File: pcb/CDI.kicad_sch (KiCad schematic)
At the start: 32 parts, among them Q1 MMBT2222A, Q10 MMBTA55, Q5 MMBT2222A, Q6 MMBT2222A, Q8 MMBTA55, Q9 MMBTA55

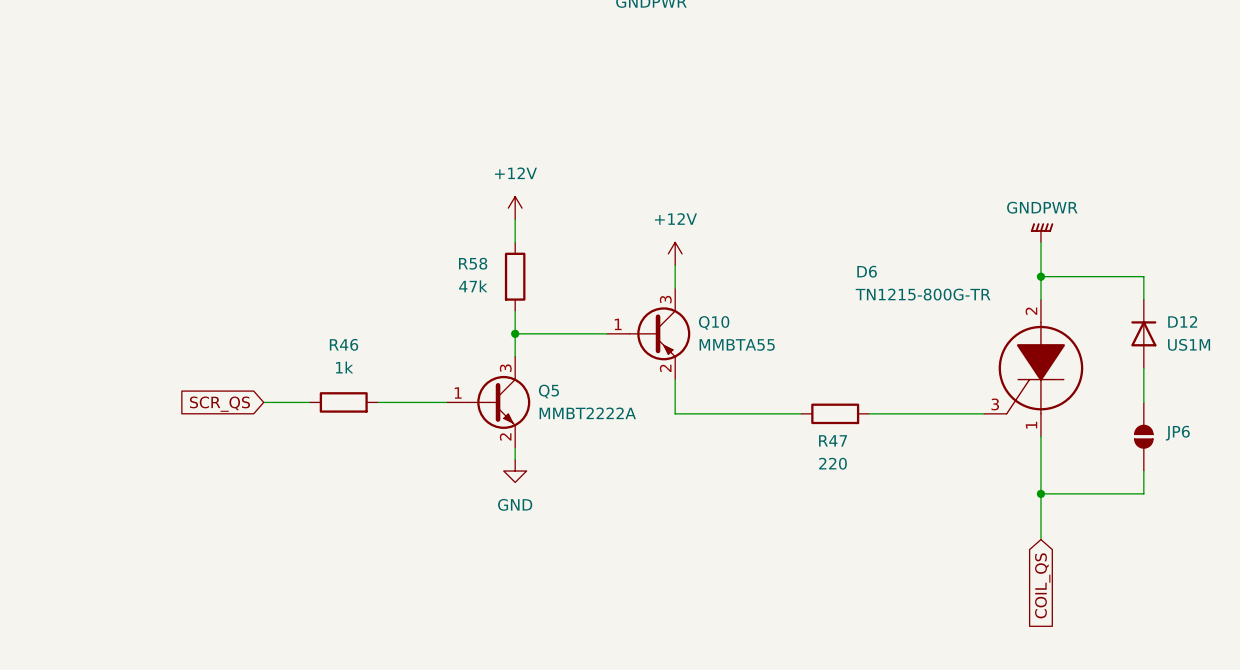
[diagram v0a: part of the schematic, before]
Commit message: changed the QS cut to use a relay
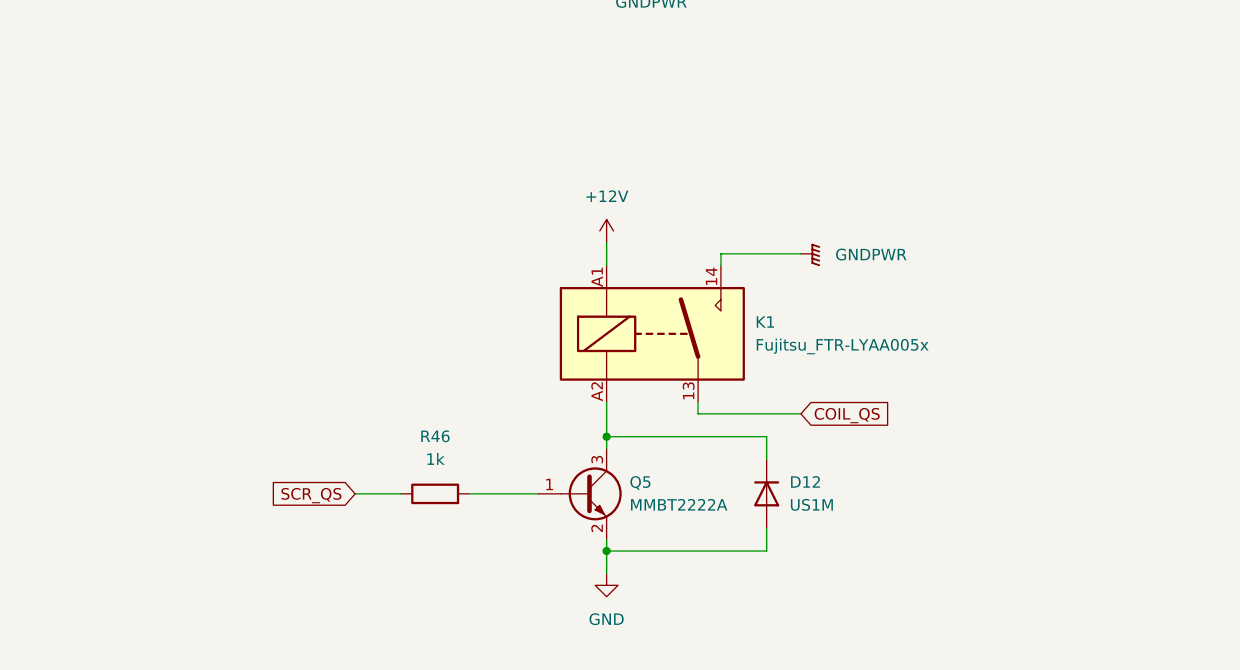
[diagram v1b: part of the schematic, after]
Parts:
- removed D6: TN1215-800G-TR, SamacSys_Parts:TN1215800GTR, symbol SamacSys_Parts:TN1215-800G-TR
- removed JP6: SolderJumper_2_Open, Jumper:SolderJumper-2_P1.3mm_Open_RoundedPad1.0x1.5mm, symbol Jumper:SolderJumper_2_Open
- removed Q10: MMBTA55, Package_TO_SOT_SMD:SOT-23, symbol Transistor_BJT:MMBTA56
- removed R47: 220, Resistor_THT:R_Axial_DIN0204_L3.6mm_D1.6mm_P1.90mm_Vertical, symbol Device:R
- removed R58: 47k, Resistor_THT:R_Axial_DIN0204_L3.6mm_D1.6mm_P1.90mm_Vertical, symbol Device:R
- added K1: Fujitsu_FTR-LYAA005x, Relay_THT:Relay_SPST-NO_Fujitsu_FTR-LYAA005x_FormA_Vertical, symbol Relay:Fujitsu_FTR-LYAA005x
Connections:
- net +12V: now also K1.A1
- net COIL_QS: now also K1.13
- net GND: now also D12.2 (A)
- net GNDPWR: now also K1.14; no longer D12.1 (K)
- net at Q5.3 (C): now also D12.1 (K), K1.A2
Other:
- moved on the sheet: D12, Q5, R46

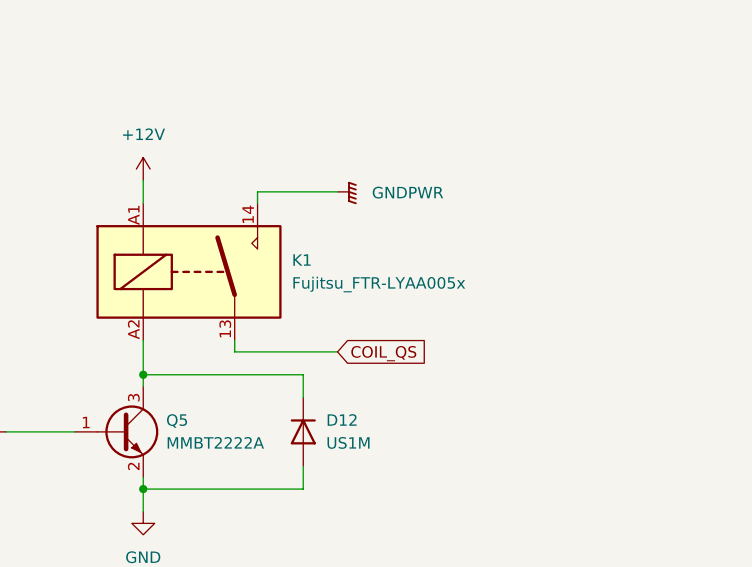
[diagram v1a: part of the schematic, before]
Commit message: added custom footprint for external relay
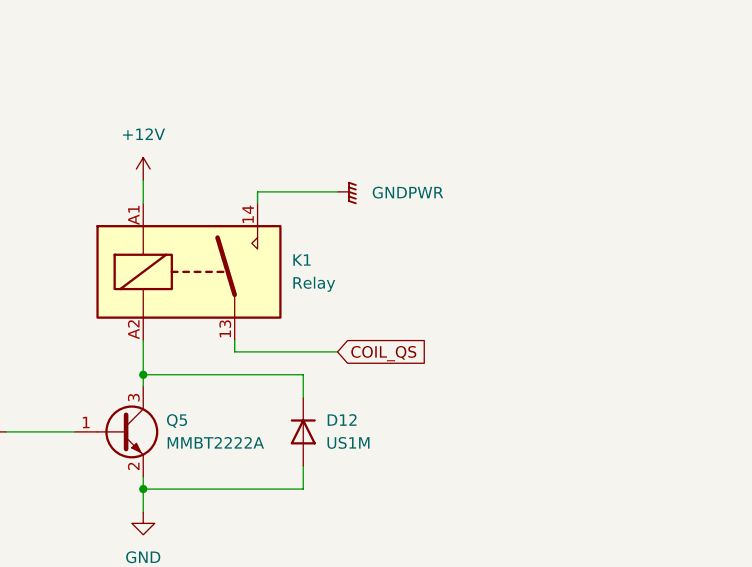
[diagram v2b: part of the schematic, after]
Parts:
- K1: value Fujitsu_FTR-LYAA005x -> Relay; footprint Relay_THT:Relay_SPST-NO_Fujitsu_FTR-LYAA005x_FormA_Vertical -> Custom:Ext_Relay
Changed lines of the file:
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@@
 			)
 		)
-		(property "Value" "Fujitsu_FTR-LYAA005x"
+		(property "Value" "Relay"
 			(at 220.98 125.7299 0)
 			(effects
@@
 			)
 		)
-		(property "Footprint" "Relay_THT:Relay_SPST-NO_Fujitsu_FTR-LYAA005x_FormA_Vertical"
+		(property "Footprint" "Custom:Ext_Relay"
 			(at 220.98 125.73 0)
 			(effects

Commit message: added DNP for fabrication and 2P molex connector, minor fixes
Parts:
- removed R57: 10k, Resistor_THT:R_Axial_DIN0204_L3.6mm_D1.6mm_P1.90mm_Vertical, symbol Device:R
- added R45: 10k, Resistor_SMD:R_0603_1608Metric, symbol Device:R
- added TP30, TP31: TestPoint, Connector_PinHeader_2.54mm:PinHeader_1x01_P2.54mm_Vertical, symbol Connector:TestPoint
- R13, R49, R56: footprint Resistor_THT:R_Axial_DIN0204_L3.6mm_D1.6mm_P1.90mm_Vertical -> Resistor_SMD:R_0603_1608Metric
- TP10, TP11, TP19, TP9: footprint Connector_PinHeader_1.00mm:PinHeader_1x01_P1.00mm_Vertical -> Connector_PinHeader_2.54mm:PinHeader_1x01_P2.54mm_Vertical; now not fitted
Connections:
- net +12V: now also R45.1
- net COIL_QS: now also TP31.1
- net KILL_SWITCH: now also TP30.1
- net at D13.3: now also R56.2; no longer R56.1
- net at Q1.3 (C), Q9.1 (B): now also R45.2
- net at Q8.2 (E): now also R56.1; no longer R56.2

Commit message: added pull-downs to QS stuff
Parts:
- added R67, R68: 100k, Resistor_SMD:R_0603_1608Metric, symbol Device:R
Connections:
- net +12V: now also D12.1 (K)
- net GND: now also R67.2, R68.2; no longer D12.2 (A)
- net at K1.A2, Q5.3 (C): now also D12.2 (A); no longer D12.1 (K)
- net at Q6.1 (B), R48.2: now also R68.1
- net at Q5.1 (B), R46.2: now also R67.1
- net SCR_QS renamed RELAY_QS
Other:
- moved on the sheet: D12

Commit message: removed GNDPWR
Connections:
- net GNDPWR is gone; now on net GND: D13.1, D2.1, JP4.1 (A), JP5.1 (A), K1.14, R18.1

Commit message: changed THT to SMD for both resistors and capacitors since they will be replaced by hand with soldering tweezers
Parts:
- C9: footprint Capacitor_THT:C_Axial_L12.0mm_D7.5mm_P20.00mm_Horizontal -> Capacitor_THT:C_Axial_L17.0mm_D6.5mm_P20.00mm_Horizontal
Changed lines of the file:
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@@
 		(color 0 0 0 0)
 	)
-	(junction
-		(at 232.41 64.6071)
-		(diameter 0)
-		(color 0 0 0 0)
-	)
 	(wire
 		(pts
@@
 	(wire
 		(pts
-			(xy 232.41 64.6071) (xy 232.41 64.77)
-		)
-		(stroke
-			(width 0)
-			(type default)
-		)
-	)
-	(wire
-		(pts
 			(xy 146.05 52.07) (xy 146.05 54.61)
 		)
@@
 	(wire
 		(pts
-			(xy 232.41 62.23) (xy 232.41 64.6071)
+			(xy 232.41 62.23) (xy 232.41 64.77)
 		)
 		(stroke
@@
 	(symbol
 		(lib_id "power:GND")
-		(at 232.41 64.6071 0)
+		(at 232.41 64.77 0)
 		(unit 1)
 		(exclude_from_sim no)
@@
 		(dnp no)
 		(property "Reference" "#PWR020"
-			(at 232.41 70.9571 0)
+			(at 232.41 71.12 0)
 			(effects
 				(font
@@
 		)
 		(property "Value" "GND"
-			(at 230.378 69.1791 0)
+			(at 230.378 69.342 0)
 			(effects
 				(font
@@
 		)
 		(property "Footprint" ""
-			(at 232.41 64.6071 0)
+			(at 232.41 64.77 0)
 			(effects
 				(font
@@
 		)
 		(property "Datasheet" ""
-			(at 232.41 64.6071 0)
+			(at 232.41 64.77 0)
 			(effects
 				(font
@@
 		)
 		(property "Description" "Power symbol creates a global label with name \"GND\" , ground"
-			(at 232.41 64.6071 0)
+			(at 232.41 64.77 0)
 			(effects
 				(font
@@
 			)
 		)
-		(property "Footprint" "Capacitor_THT:C_Axial_L12.0mm_D7.5mm_P20.00mm_Horizontal"
+		(property "Footprint" "Capacitor_THT:C_Axial_L17.0mm_D6.5mm_P20.00mm_Horizontal"
 			(at 245.11 39.6748 0)
 			(effects
@@
 			)
 		)
-		(property "Description" "300V"
+		(property "Description" "400V"
 			(at 241.3 36.576 90)
 			(effects

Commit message: updated SCRs footprint
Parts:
- D13, D2: footprint SamacSys_Parts:TN1215800GTR -> Package_TO_SOT_SMD:TO-263-2
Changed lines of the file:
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@@
 			)
 		)
-		(property "Footprint" "SamacSys_Parts:TN1215800GTR"
+		(property "Footprint" "Package_TO_SOT_SMD:TO-263-2"
 			(at 104.14 138.43 0)
 			(effects
@@
 			)
 		)
-		(property "Footprint" "SamacSys_Parts:TN1215800GTR"
+		(property "Footprint" "Package_TO_SOT_SMD:TO-263-2"
 			(at 201.93 63.5 0)
 			(effects

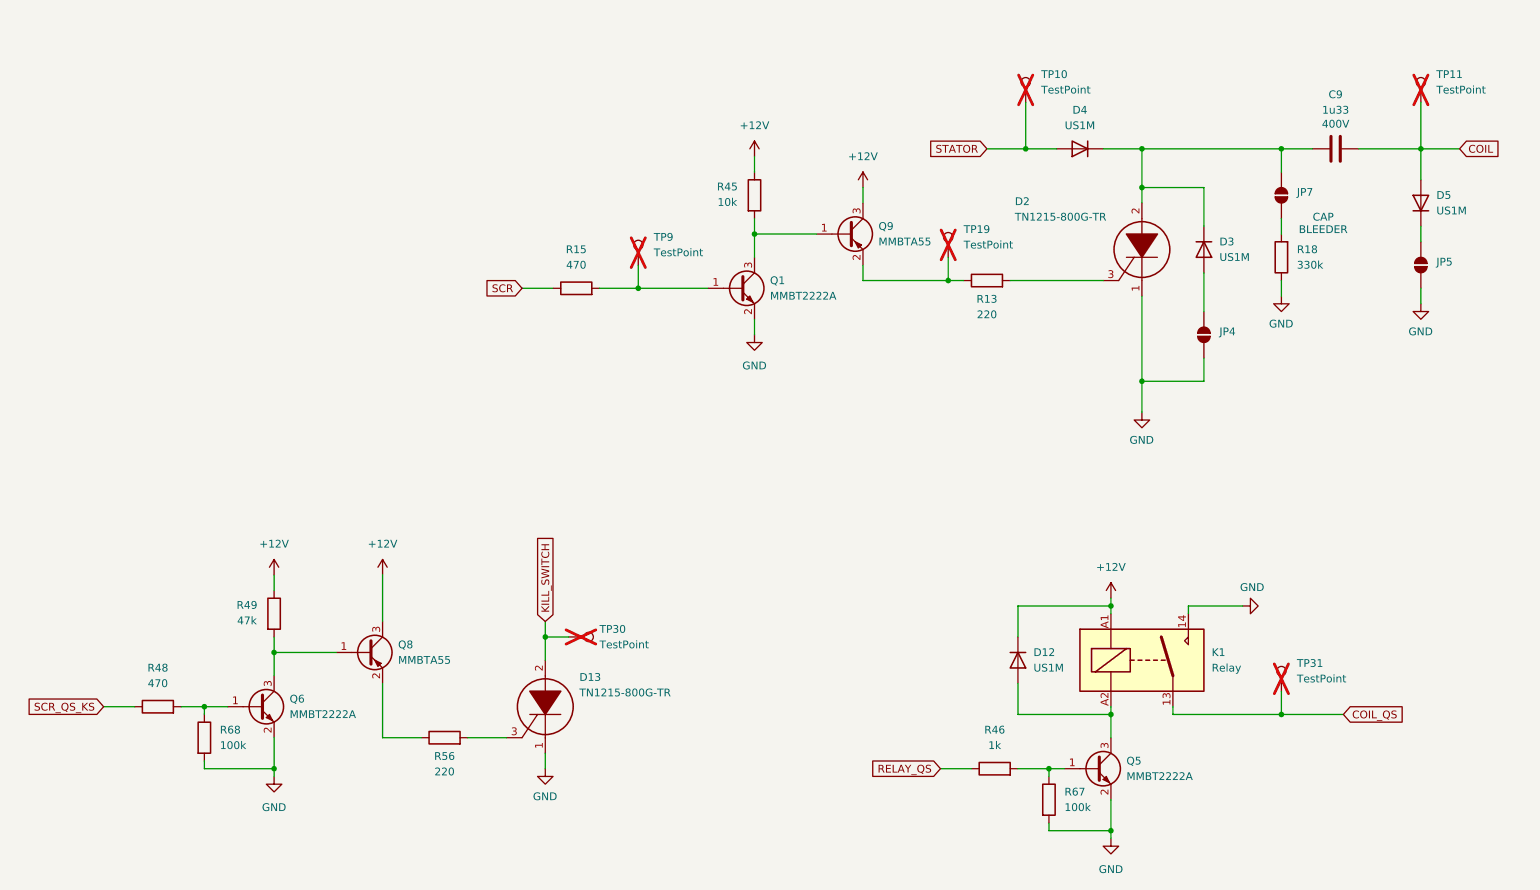
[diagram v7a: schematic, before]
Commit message: revision 2.0: changed components numeration
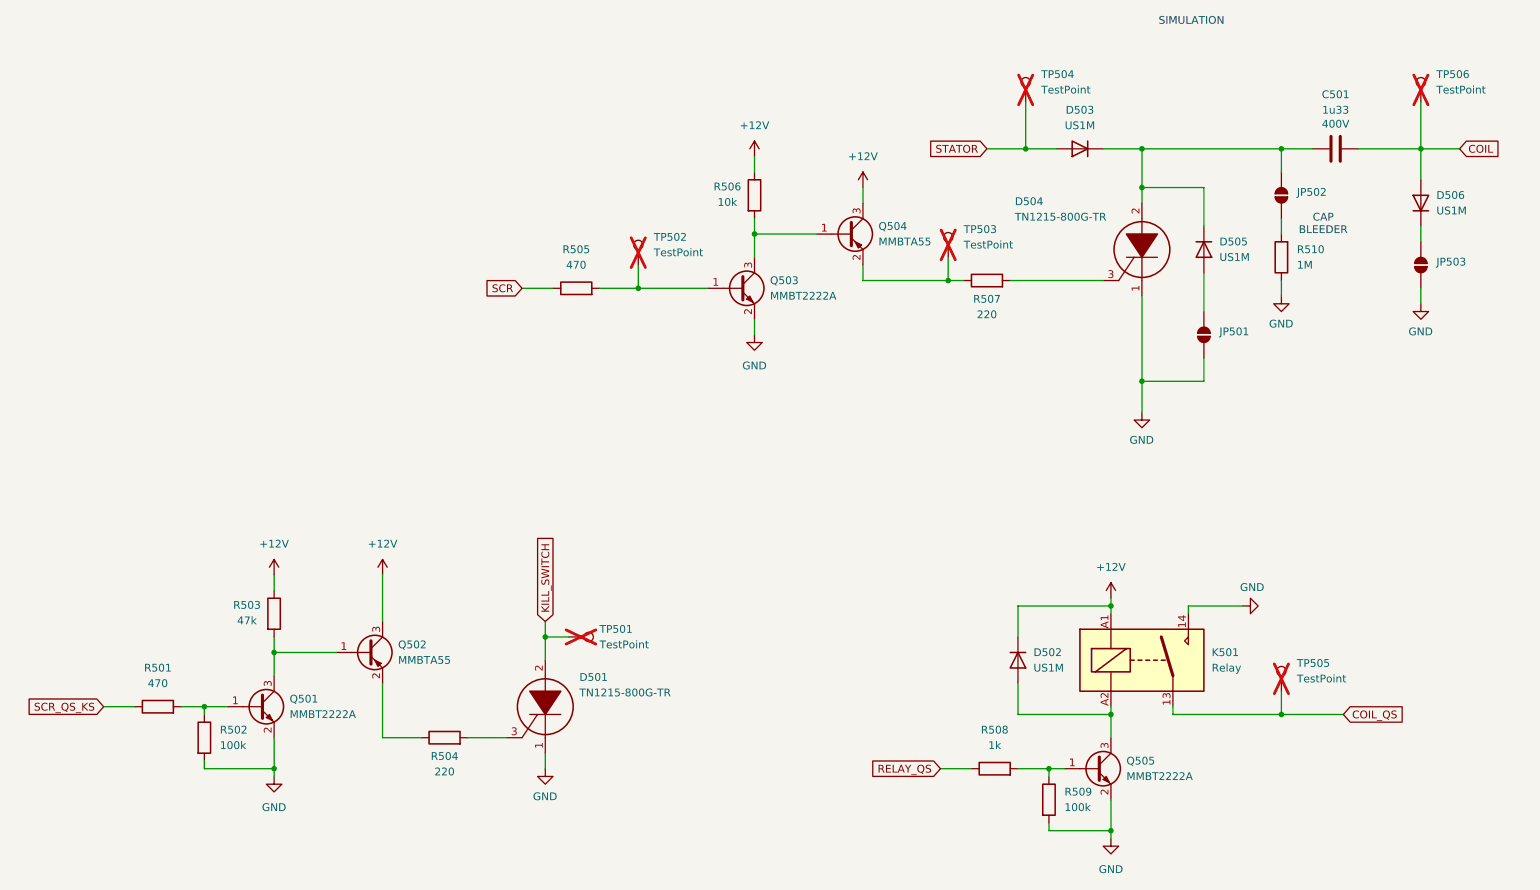
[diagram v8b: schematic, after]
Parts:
- R510: renamed from R18; value 330k -> 1M
- renumbered C9 to C501, D13 to D501, D12 to D502, D4 to D503, D2 to D504, D3 to D505, D5 to D506, JP4 to JP501, JP7 to JP502, JP5 to JP503, K1 to K501, Q6 to Q501, Q8 to Q502, Q1 to Q503, Q9 to Q504, Q5 to Q505, R48 to R501, R68 to R502, R49 to R503, R56 to R504, R15 to R505, R45 to R506, R13 to R507, R46 to R508, R67 to R509, TP30 to TP501, TP9 to TP502, TP19 to TP503, TP10 to TP504, TP31 to TP505, TP11 to TP506
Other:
- note added: "SIMULATION"
